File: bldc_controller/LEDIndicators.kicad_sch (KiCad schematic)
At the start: 4 parts

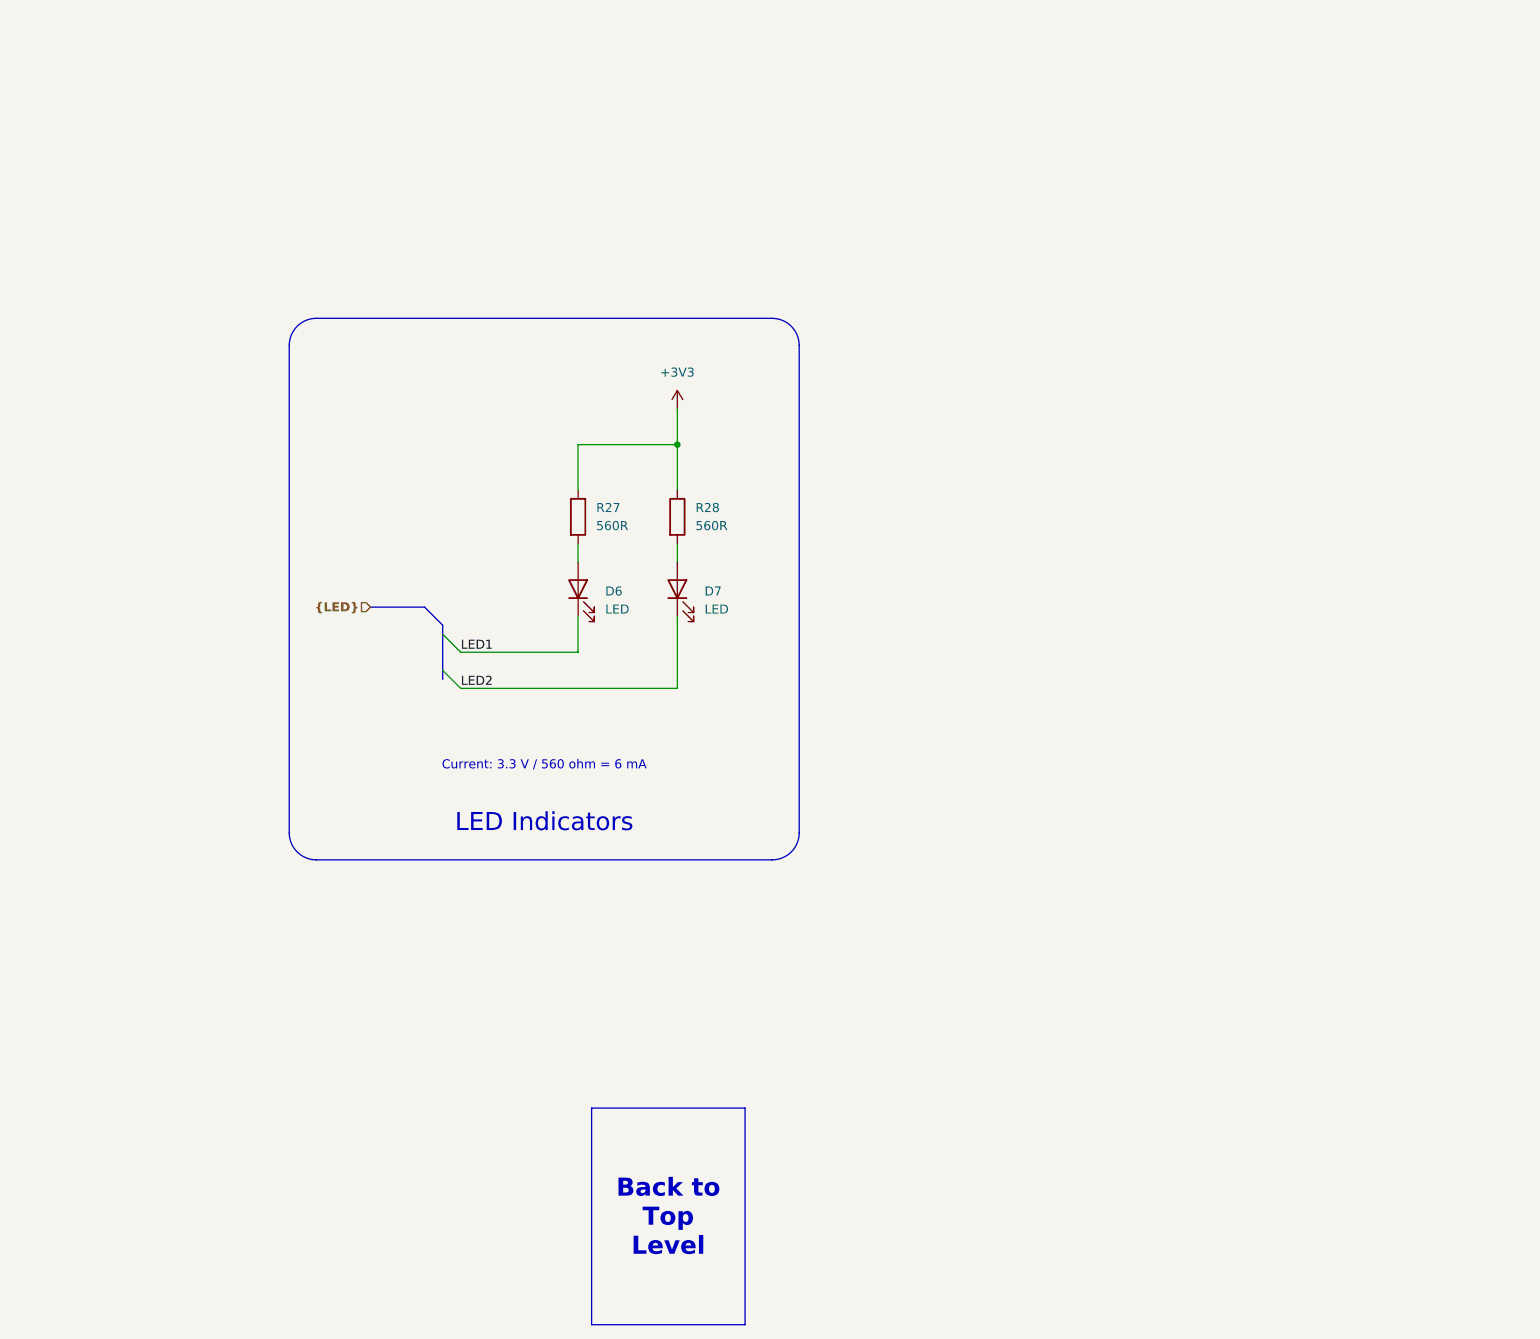
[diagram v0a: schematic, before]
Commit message: added temporary footprints and deleted extra files
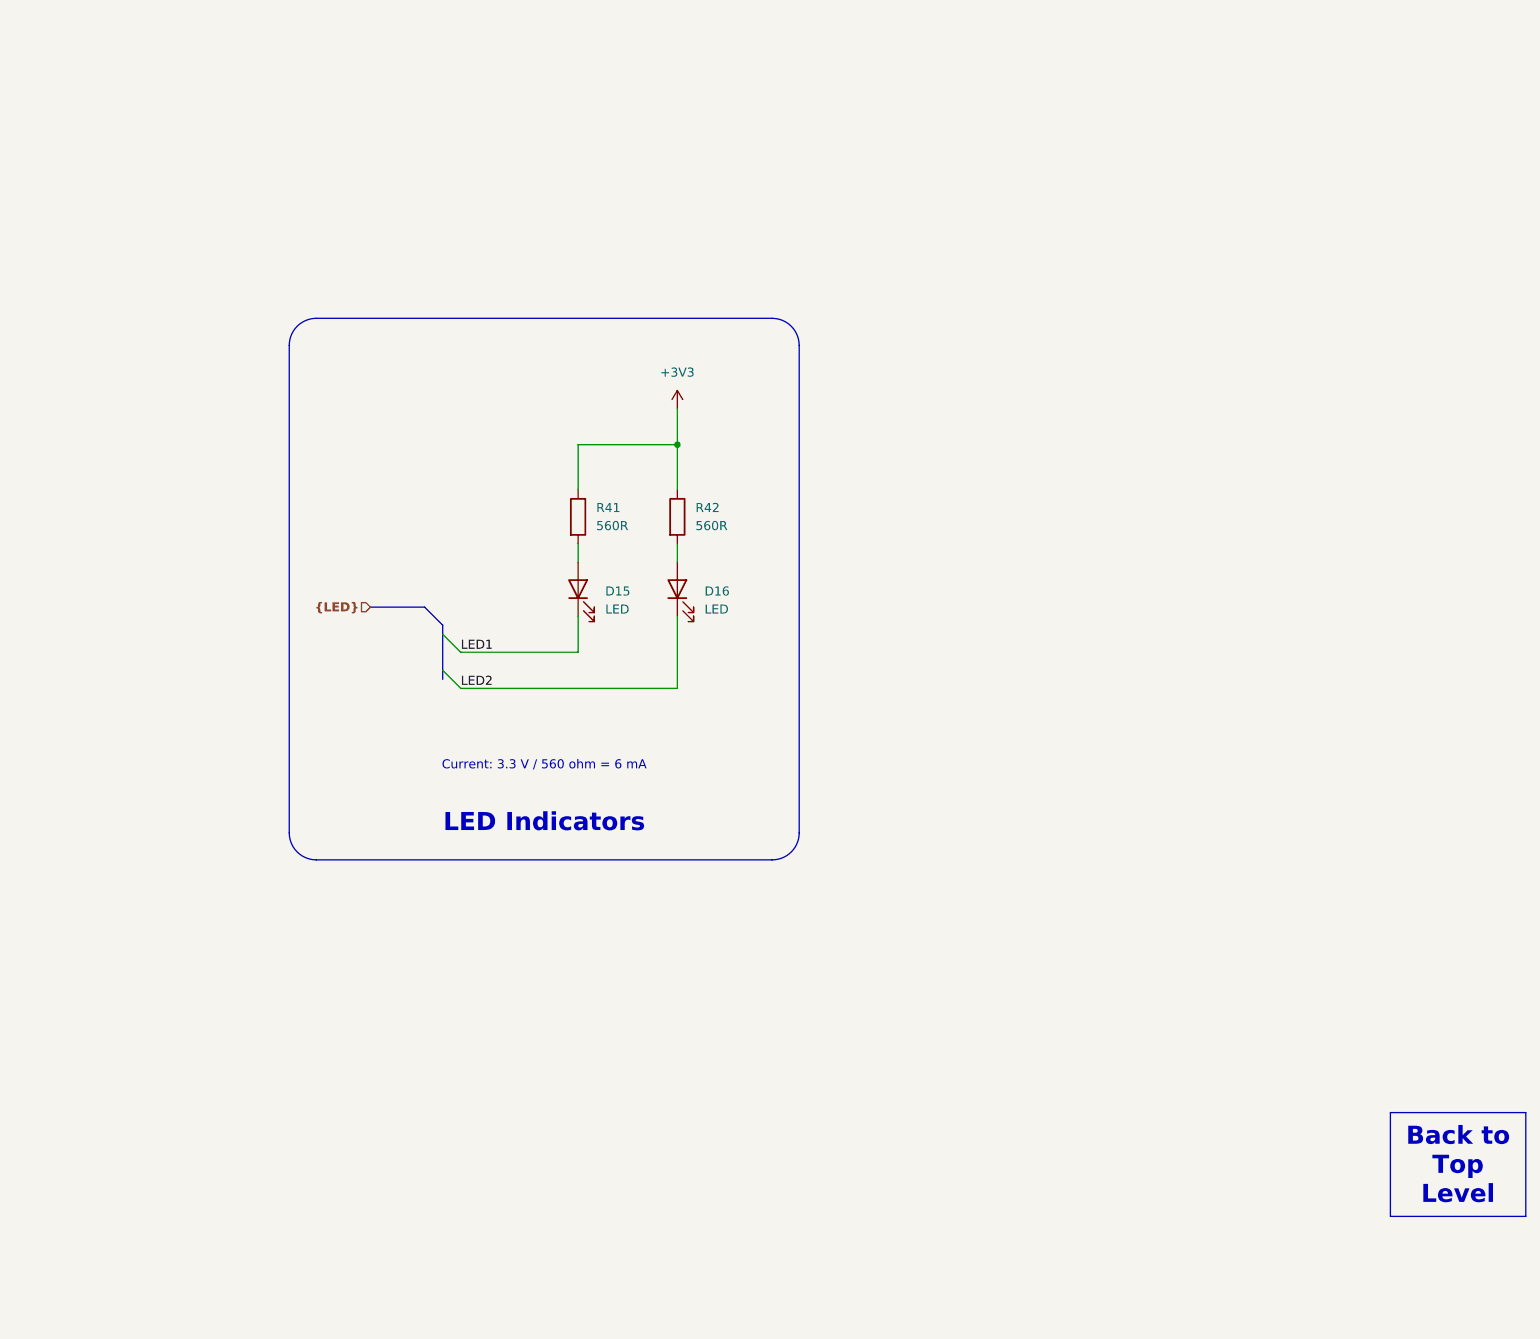
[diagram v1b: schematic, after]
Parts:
- D15: renamed from D6; footprint (none) -> LED_SMD:LED_0603_1608Metric
- D16: renamed from D7; footprint (none) -> LED_SMD:LED_0603_1608Metric
- R41: renamed from R27; footprint (none) -> Resistor_SMD:R_0402_1005Metric
- R42: renamed from R28; footprint (none) -> Resistor_SMD:R_0402_1005Metric
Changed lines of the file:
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@@
     (stroke (width -0.0001) (type default))
     (fill (type none))
-    (effects (font (size 2.54 2.54) (color 0 0 0 1)) (justify bottom))
-  )
-  (text_box "Back to Top Level"
-    (at 153.035 165.735 0) (size 21.59 30.48)
-    (stroke (width 0) (type default) (color 0 0 0 1))
-    (fill (type color) (color 0 0 0 0.1))
-    (effects (font (size 2.54 2.54) (thickness 0.508) bold (color 0 0 0 1)) (href "#1"))
+    (effects (font (size 2.54 2.54) (thickness 0.508) bold (color 0 0 0 1)) (justify bottom))
   )
   (text_box "Current: 3.3 V / 560 ohm = 6 mA"
@@
     (fill (type none))
     (effects (font (size 1.27 1.27)) (justify top))
+  )
+  (text_box "Back to Top Level"
+    (at 265.43 166.37 0) (size 19.05 14.605)
+    (stroke (width 0) (type default) (color 0 0 0 1))
+    (fill (type color) (color 0 0 0 0.1))
+    (effects (font (size 2.54 2.54) (thickness 0.508) bold (color 0 0 0 1)) (href "#1"))
   )
   (label "LED1" (at 134.62 101.6 0) (fields_autoplaced)
@@
   (symbol (lib_id "Device:R") (at 165.1 82.55 0) (unit 1)
     (in_bom yes) (on_board yes) (dnp no) (fields_autoplaced)
-    (property "Reference" "R28" (at 167.64 81.28 0)
+    (property "Reference" "R42" (at 167.64 81.28 0)
       (effects (font (size 1.27 1.27)) (justify left))
     )
@@
       (effects (font (size 1.27 1.27)) (justify left))
     )
-    (property "Footprint" "" (at 163.322 82.55 90)
+    (property "Footprint" "Resistor_SMD:R_0402_1005Metric" (at 163.322 82.55 90)
       (effects (font (size 1.27 1.27)) hide)
     )
@@
       (project "bldc_controller"
         (path "/0650c7a8-acba-429c-9f8e-eec0baf0bc1c/5b60f270-becd-4ec3-b763-258df225fc82"
-          (reference "R28") (unit 1)
+          (reference "R42") (unit 1)
         )
       )
@@
   (symbol (lib_id "Device:R") (at 151.13 82.55 0) (unit 1)
     (in_bom yes) (on_board yes) (dnp no) (fields_autoplaced)
-    (property "Reference" "R27" (at 153.67 81.28 0)
+    (property "Reference" "R41" (at 153.67 81.28 0)
       (effects (font (size 1.27 1.27)) (justify left))
     )
@@
       (effects (font (size 1.27 1.27)) (justify left))
     )
-    (property "Footprint" "" (at 149.352 82.55 90)
+    (property "Footprint" "Resistor_SMD:R_0402_1005Metric" (at 149.352 82.55 90)
       (effects (font (size 1.27 1.27)) hide)
     )
@@
       (project "bldc_controller"
         (path "/0650c7a8-acba-429c-9f8e-eec0baf0bc1c/5b60f270-becd-4ec3-b763-258df225fc82"
-          (reference "R27") (unit 1)
+          (reference "R41") (unit 1)
         )
       )
@@
   (symbol (lib_id "power:+3V3") (at 165.1 67.31 0) (unit 1)
     (in_bom yes) (on_board yes) (dnp no) (fields_autoplaced)
-    (property "Reference" "#PWR050" (at 165.1 71.12 0)
+    (property "Reference" "#PWR070" (at 165.1 71.12 0)
       (effects (font (size 1.27 1.27)) hide)
     )
@@
       (project "bldc_controller"
         (path "/0650c7a8-acba-429c-9f8e-eec0baf0bc1c/5b60f270-becd-4ec3-b763-258df225fc82"
-          (reference "#PWR050") (unit 1)
+          (reference "#PWR070") (unit 1)
         )
       )
@@
   (symbol (lib_id "Device:LED") (at 165.1 92.71 90) (unit 1)
     (in_bom yes) (on_board yes) (dnp no) (fields_autoplaced)
-    (property "Reference" "D7" (at 168.91 93.0275 90)
+    (property "Reference" "D16" (at 168.91 93.0275 90)
       (effects (font (size 1.27 1.27)) (justify right))
     )
@@
       (effects (font (size 1.27 1.27)) (justify right))
     )
-    (property "Footprint" "" (at 165.1 92.71 0)
+    (property "Footprint" "LED_SMD:LED_0603_1608Metric" (at 165.1 92.71 0)
       (effects (font (size 1.27 1.27)) hide)
     )
@@
       (project "bldc_controller"
         (path "/0650c7a8-acba-429c-9f8e-eec0baf0bc1c/5b60f270-becd-4ec3-b763-258df225fc82"
-          (reference "D7") (unit 1)
+          (reference "D16") (unit 1)
         )
       )
@@
   (symbol (lib_id "Device:LED") (at 151.13 92.71 90) (unit 1)
     (in_bom yes) (on_board yes) (dnp no) (fields_autoplaced)
-    (property "Reference" "D6" (at 154.94 93.0275 90)
+    (property "Reference" "D15" (at 154.94 93.0275 90)
       (effects (font (size 1.27 1.27)) (justify right))
     )
@@
       (effects (font (size 1.27 1.27)) (justify right))
     )
-    (property "Footprint" "" (at 151.13 92.71 0)
+    (property "Footprint" "LED_SMD:LED_0603_1608Metric" (at 151.13 92.71 0)
       (effects (font (size 1.27 1.27)) hide)
     )
@@
       (project "bldc_controller"
         (path "/0650c7a8-acba-429c-9f8e-eec0baf0bc1c/5b60f270-becd-4ec3-b763-258df225fc82"
-          (reference "D6") (unit 1)
+          (reference "D15") (unit 1)
         )
       )

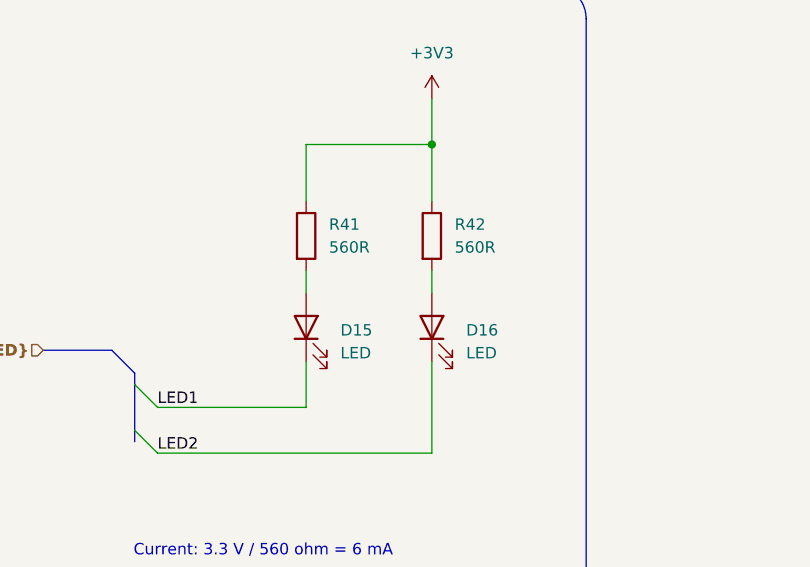
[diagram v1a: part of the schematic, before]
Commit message: added IPC-7351 compliant footprints and started routing
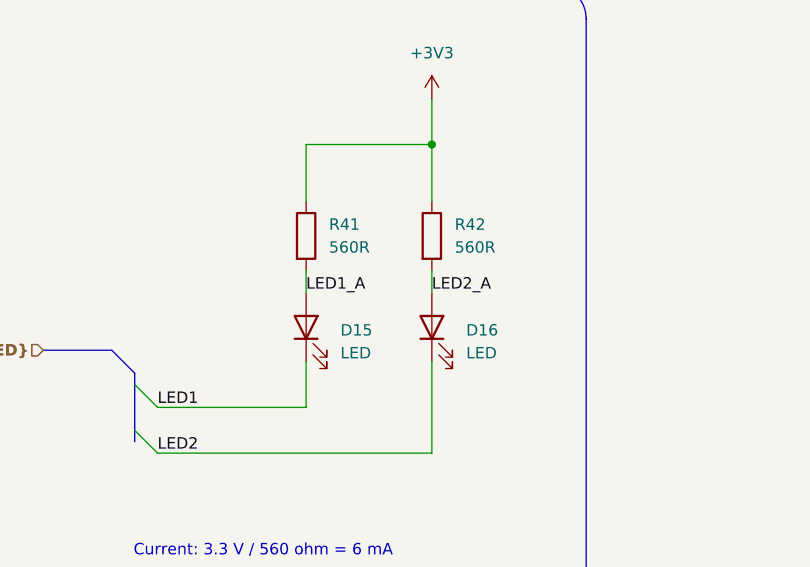
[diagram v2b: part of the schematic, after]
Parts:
- R41, R42: footprint Resistor_SMD:R_0402_1005Metric -> 0_resistor_smd:R_0402_1005_DensityHigh
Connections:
- net LED2_A: now reaches D16.2 (A), R42.2
- net LED1_A: now reaches D15.2 (A), R41.2
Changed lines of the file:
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@@
     (effects (font (size 2.54 2.54) (thickness 0.508) bold (color 0 0 0 1)) (href "#1"))
+  )
+  (label "LED1_A" (at 151.13 88.9 0) (fields_autoplaced)
+    (effects (font (size 1.27 1.27)) (justify left bottom))
   )
   (label "LED1" (at 134.62 101.6 0) (fields_autoplaced)
@@
   )
   (label "LED2" (at 134.62 106.68 0) (fields_autoplaced)
+    (effects (font (size 1.27 1.27)) (justify left bottom))
+  )
+  (label "LED2_A" (at 165.1 88.9 0) (fields_autoplaced)
     (effects (font (size 1.27 1.27)) (justify left bottom))
   )
@@
       (effects (font (size 1.27 1.27)) (justify left))
     )
-    (property "Footprint" "Resistor_SMD:R_0402_1005Metric" (at 163.322 82.55 90)
+    (property "Footprint" "0_resistor_smd:R_0402_1005_DensityHigh" (at 163.322 82.55 90)
       (effects (font (size 1.27 1.27)) hide)
     )
@@
       (effects (font (size 1.27 1.27)) (justify left))
     )
-    (property "Footprint" "Resistor_SMD:R_0402_1005Metric" (at 149.352 82.55 90)
+    (property "Footprint" "0_resistor_smd:R_0402_1005_DensityHigh" (at 149.352 82.55 90)
       (effects (font (size 1.27 1.27)) hide)
     )
@@
   (symbol (lib_id "power:+3V3") (at 165.1 67.31 0) (unit 1)
     (in_bom yes) (on_board yes) (dnp no) (fields_autoplaced)
-    (property "Reference" "#PWR070" (at 165.1 71.12 0)
+    (property "Reference" "#PWR069" (at 165.1 71.12 0)
       (effects (font (size 1.27 1.27)) hide)
     )
@@
       (project "bldc_controller"
         (path "/0650c7a8-acba-429c-9f8e-eec0baf0bc1c/5b60f270-becd-4ec3-b763-258df225fc82"
-          (reference "#PWR070") (unit 1)
+          (reference "#PWR069") (unit 1)
         )
       )

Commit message: might have fixed net issue, added dxf and svgs
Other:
- moved on the sheet: D15, D16, R41, R42

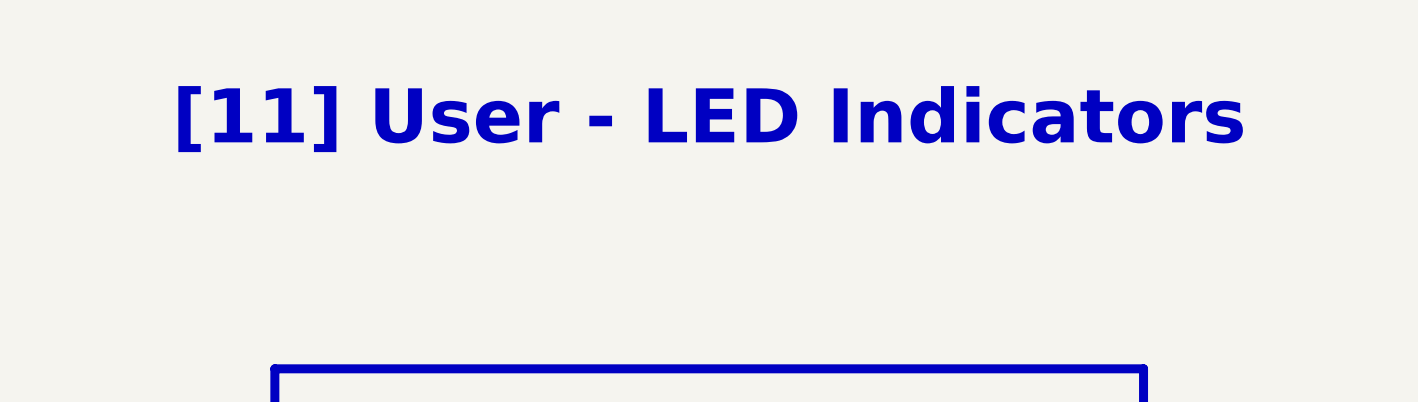
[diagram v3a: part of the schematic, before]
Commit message: Replaced 3v3 buck with WSON package alternative. Will back-annotate components
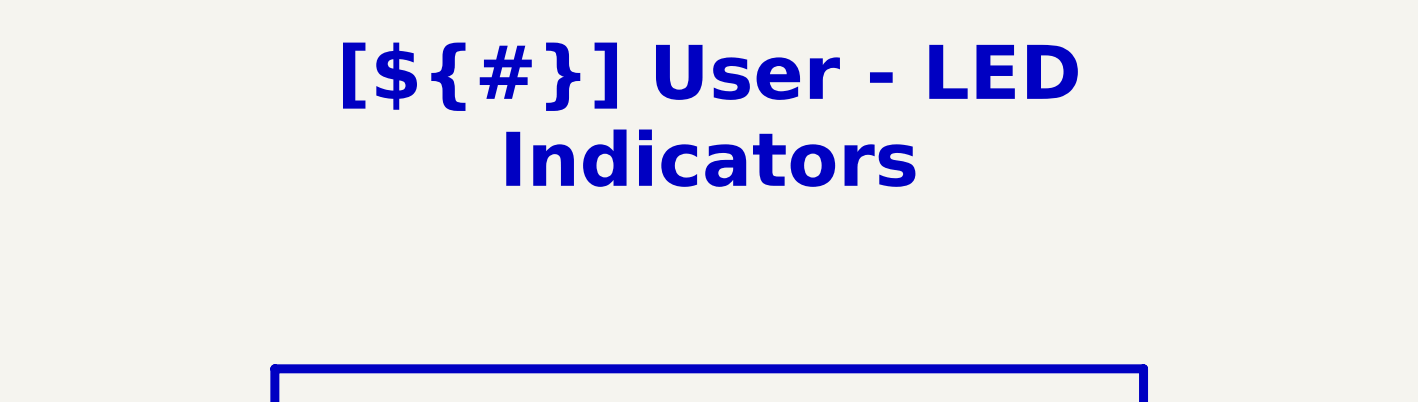
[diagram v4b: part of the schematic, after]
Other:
- company: EPFL Xplore -> ${COMPANY}
- title: LED Indicators -> User - LED Indicators
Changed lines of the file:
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@@
   (paper "A4")
   (title_block
-    (title "LED Indicators")
+    (title "User - LED Indicators")
     (date "2023-10-15")
-    (rev "1.0")
-    (company "EPFL Xplore")
-    (comment 3 "Author: Vincent Nguyen")
+    (rev "${REVISION}")
+    (company "${COMPANY}")
+    (comment 3 "Author: ${AUTHOR}")
   )
   (junction (at 162.56 68.58) (diameter 0) (color 0 0 0 0)
@@
     (fill (type none))
   )
-  (text_box "[11] User - LED Indicators"
+  (text_box "[${#}] ${TITLE}"
     (at 80.01 16.51 0) (size 137.16 12.7)
     (stroke (width -0.0001) (type default))
